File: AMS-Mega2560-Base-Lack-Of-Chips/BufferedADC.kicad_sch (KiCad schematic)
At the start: 5 parts, among them IC20 OPA4340UA

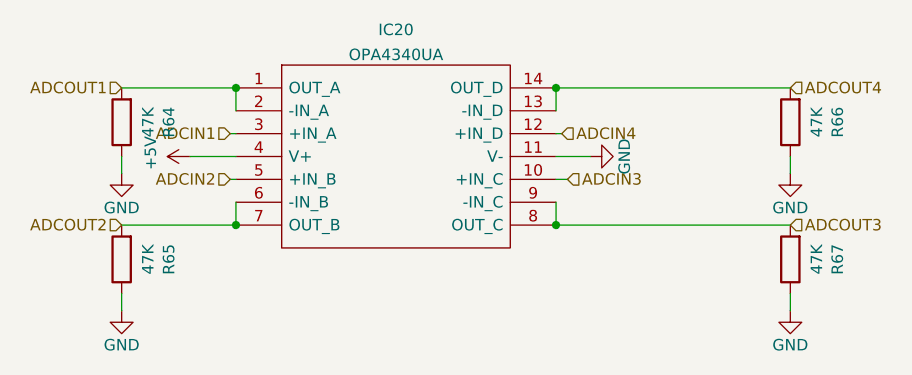
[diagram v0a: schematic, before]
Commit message: replaced the RTD with adafruit Dev boards which are easy to get at the moment.
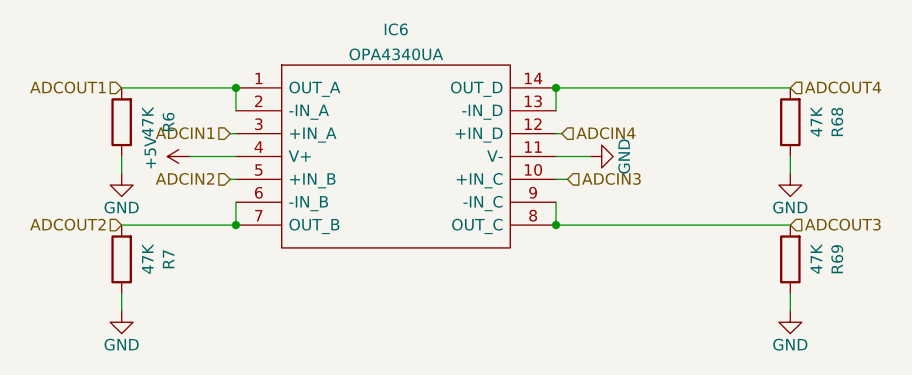
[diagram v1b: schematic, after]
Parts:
- renumbered IC20 to IC6, R64 to R6, R66 to R68, R67 to R69, R65 to R7
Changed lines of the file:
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@@
   (symbol (lib_id "Device:R") (at 118.745 62.865 180)
     (in_bom yes) (on_board yes)
-    (property "Reference" "R64" (id 0) (at 124.0028 62.865 90))
+    (property "Reference" "R6" (id 0) (at 124.0028 62.865 90))
     (property "Value" "47K" (id 1) (at 121.6914 62.865 90))
     (property "Footprint" "Resistor_THT:R_Axial_DIN0207_L6.3mm_D2.5mm_P2.54mm_Vertical" (id 2) (at 120.523 62.865 90)
@@
   (symbol (lib_id "Samac_Sys:OPA4340UA") (at 131.445 59.055 0)
     (in_bom yes) (on_board yes) (fields_autoplaced)
-    (property "Reference" "IC20" (id 0) (at 149.225 52.5993 0))
+    (property "Reference" "IC6" (id 0) (at 149.225 52.5993 0))
     (property "Value" "OPA4340UA" (id 1) (at 149.225 55.3744 0))
     (property "Footprint" "SOIC127P600X175-14N" (id 2) (at 163.195 56.515 0)
@@
   (symbol (lib_id "power:GND") (at 170.815 66.675 90)
     (in_bom yes) (on_board yes)
-    (property "Reference" "#PWR085" (id 0) (at 177.165 66.675 0)
+    (property "Reference" "#PWR0143" (id 0) (at 177.165 66.675 0)
       (effects (font (size 1.27 1.27)) hide)
     )
@@
   (symbol (lib_id "Device:R") (at 118.745 78.105 180)
     (in_bom yes) (on_board yes)
-    (property "Reference" "R65" (id 0) (at 124.0028 78.105 90))
+    (property "Reference" "R7" (id 0) (at 124.0028 78.105 90))
     (property "Value" "47K" (id 1) (at 121.6914 78.105 90))
     (property "Footprint" "Resistor_THT:R_Axial_DIN0207_L6.3mm_D2.5mm_P2.54mm_Vertical" (id 2) (at 120.523 78.105 90)
@@
   (symbol (lib_id "power:GND") (at 118.745 68.58 0)
     (in_bom yes) (on_board yes)
-    (property "Reference" "#PWR05" (id 0) (at 118.745 74.93 0)
+    (property "Reference" "#PWR0144" (id 0) (at 118.745 74.93 0)
       (effects (font (size 1.27 1.27)) hide)
     )
@@
   (symbol (lib_id "power:+5V") (at 126.365 66.675 90)
     (in_bom yes) (on_board yes)
-    (property "Reference" "#PWR082" (id 0) (at 130.175 66.675 0)
+    (property "Reference" "#PWR0142" (id 0) (at 130.175 66.675 0)
       (effects (font (size 1.27 1.27)) hide)
     )
@@
   (symbol (lib_id "Device:R") (at 193.04 62.865 180)
     (in_bom yes) (on_board yes)
-    (property "Reference" "R66" (id 0) (at 198.2978 62.865 90))
+    (property "Reference" "R68" (id 0) (at 198.2978 62.865 90))
     (property "Value" "47K" (id 1) (at 195.9864 62.865 90))
     (property "Footprint" "Resistor_THT:R_Axial_DIN0207_L6.3mm_D2.5mm_P2.54mm_Vertical" (id 2) (at 194.818 62.865 90)
@@
   (symbol (lib_id "power:GND") (at 118.745 83.82 0)
     (in_bom yes) (on_board yes)
-    (property "Reference" "#PWR067" (id 0) (at 118.745 90.17 0)
+    (property "Reference" "#PWR0141" (id 0) (at 118.745 90.17 0)
       (effects (font (size 1.27 1.27)) hide)
     )
@@
   (symbol (lib_id "power:GND") (at 193.04 68.58 0)
     (in_bom yes) (on_board yes)
-    (property "Reference" "#PWR098" (id 0) (at 193.04 74.93 0)
+    (property "Reference" "#PWR0127" (id 0) (at 193.04 74.93 0)
       (effects (font (size 1.27 1.27)) hide)
     )
@@
   (symbol (lib_id "power:GND") (at 193.04 83.82 0)
     (in_bom yes) (on_board yes)
-    (property "Reference" "#PWR0104" (id 0) (at 193.04 90.17 0)
+    (property "Reference" "#PWR0140" (id 0) (at 193.04 90.17 0)
       (effects (font (size 1.27 1.27)) hide)
     )
@@
   (symbol (lib_id "Device:R") (at 193.04 78.105 180)
     (in_bom yes) (on_board yes)
-    (property "Reference" "R67" (id 0) (at 198.2978 78.105 90))
+    (property "Reference" "R69" (id 0) (at 198.2978 78.105 90))
     (property "Value" "47K" (id 1) (at 195.9864 78.105 90))
     (property "Footprint" "Resistor_THT:R_Axial_DIN0207_L6.3mm_D2.5mm_P2.54mm_Vertical" (id 2) (at 194.818 78.105 90)
